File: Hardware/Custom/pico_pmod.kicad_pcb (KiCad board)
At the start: 2 copper layers, 50 x 37 mm, 35 parts, among them J1 Conn_02x06_Odd_Even, J2 Conn_02x06_Odd_Even, J3 Conn_02x06_Odd_Even, J4 USB_C_Receptacle_USB2.0, J5 Conn_01x04, SW1 SW_Push, SW2 SW_Push, U1 RP2040, U2 W25Q128JVS, U3 NCP1117-3.3_SOT223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

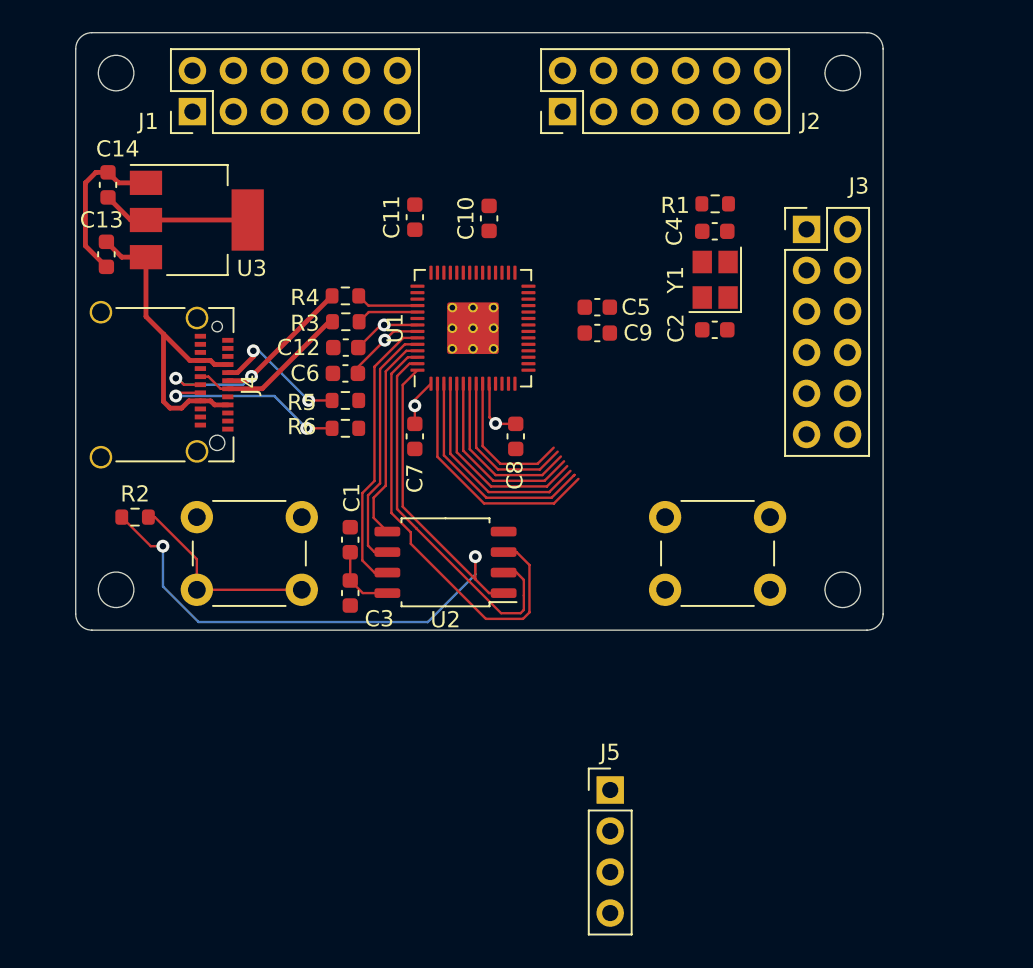
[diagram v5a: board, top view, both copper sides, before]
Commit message: PCB layout for PMOD1B and PMOD2
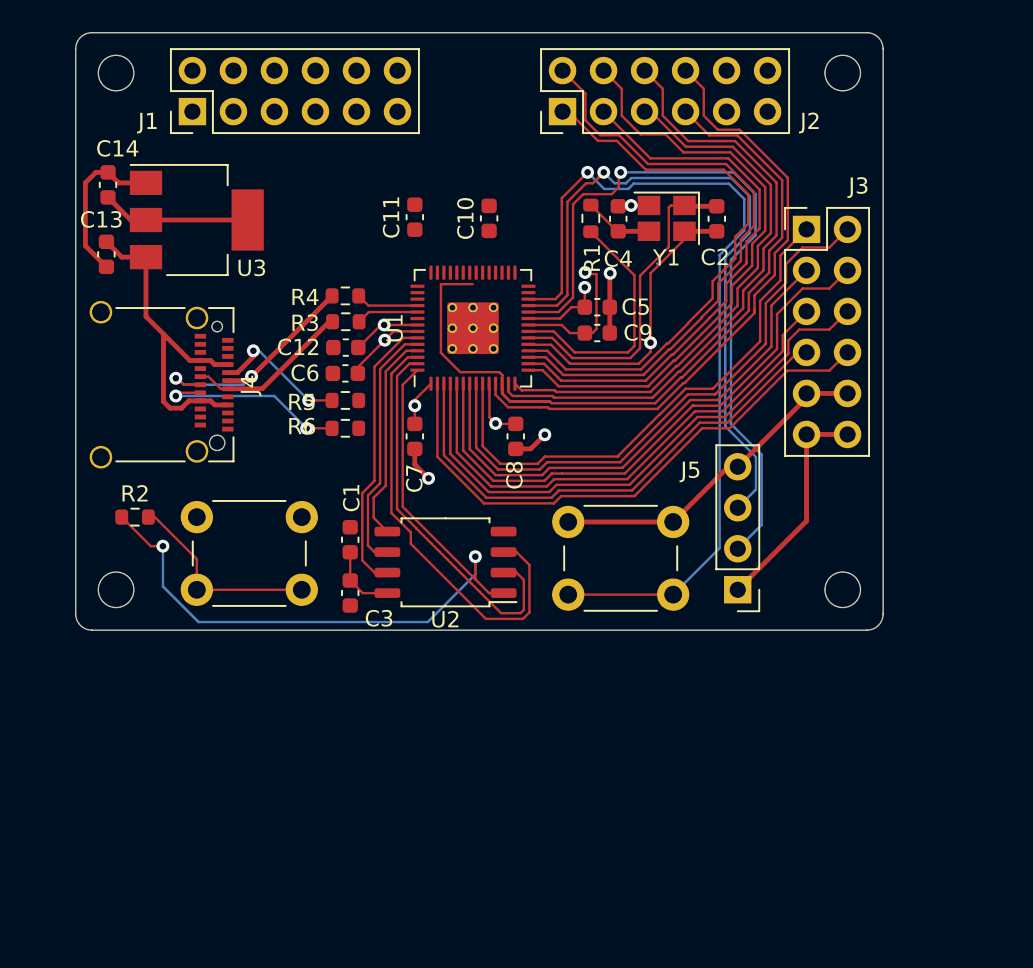
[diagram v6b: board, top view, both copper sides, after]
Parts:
- moved J5 14.7 mm to (164.0, 91.5), turned to 180 degrees
- moved R1 7.75 mm to (154.9, 68.5), turned to 90 degrees
- moved C2 6.88 mm to (162.7, 68.5), turned to 270 degrees
- moved C4 6.03 mm to (156.6, 68.5), turned to 90 degrees
- moved SW2 6.01 mm to (153.5, 87.3)
- moved Y1 4.84 mm to (159.6, 68.5), turned to 180 degrees
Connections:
- J2 pad 1: Net-(J2-Pad1) -> GPIO_15
- J2 pad 2: Net-(J2-Pad2) -> GPIO_14
- J2 pad 3: Net-(J2-Pad3) -> GPIO_13
- J2 pad 4: Net-(J2-Pad4) -> GPIO_12
- J2 pad 5: Net-(J2-Pad5) -> GPIO_11
- J2 pad 6: Net-(J2-Pad6) -> GPIO_10
- J2 pad 7: Net-(J2-Pad7) -> GPIO_9
- J2 pad 8: Net-(J2-Pad8) -> GPIO_8
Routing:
- net Pico_Run: track 0.00 -> 53.8 mm, vias 0 -> 1
- net GPIO_9: track 0.00 -> 50.3 mm
- net GND: track 10.0 -> 59.5 mm, vias 0 -> 5
- net SWCLK: track 0.00 -> 46.0 mm, vias 0 -> 1
- net SWDIO: track 0.00 -> 43.1 mm, vias 0 -> 1
- net GPIO_8: track 0.00 -> 38.9 mm
- net GPIO_10: track 0.00 -> 38.1 mm
- net GPIO_14: track 0.00 -> 37.9 mm
- net GPIO_12: track 0.00 -> 37.2 mm
- net GPIO_15: track 0.00 -> 34.7 mm
- net GPIO_11: track 0.00 -> 34.3 mm
- net GPIO_13: track 0.00 -> 34.3 mm
- net GPIO_6: track 10.0 -> 35.8 mm
- net GPIO_4: track 11.7 -> 35.5 mm
- net GPIO_7: track 9.13 -> 32.8 mm
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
